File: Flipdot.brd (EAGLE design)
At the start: 160 x 100 mm, 22 parts, among them IC1 ULN2003, IC10 ULN2003, IC11 M74HC238, IC12 M74HC238, IC13 M74HC238, IC14 TD62783_AFWG, IC15 ULN2003, IC16 TD62783_AFWG, IC17 ULN2003, IC18 M74HC238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

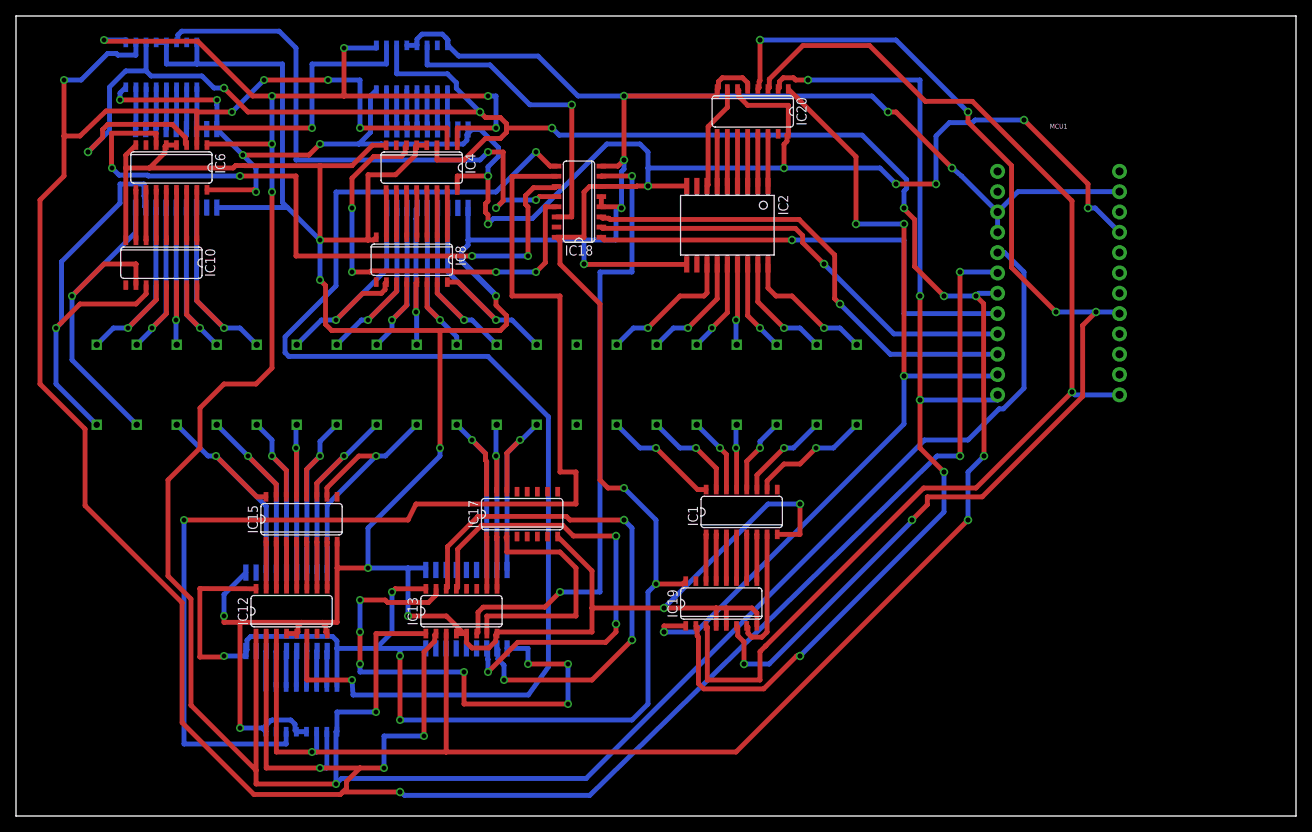
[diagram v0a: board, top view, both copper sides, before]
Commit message: Fixed trace spacing
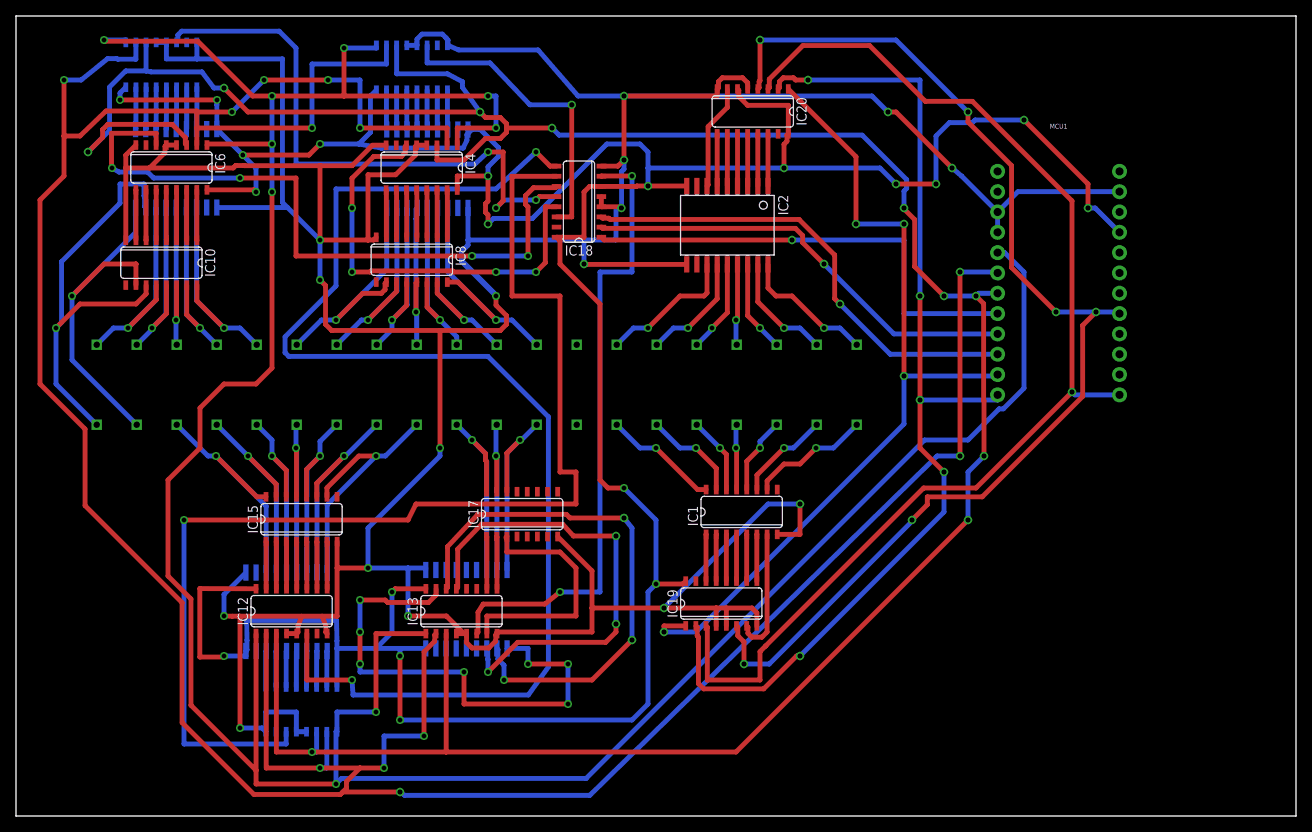
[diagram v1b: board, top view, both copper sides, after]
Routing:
- net 5V: track 407.5 -> 412.5 mm
- net GND: track 587.1 -> 590.0 mm
- net E3: track 72.7 -> 73.4 mm
